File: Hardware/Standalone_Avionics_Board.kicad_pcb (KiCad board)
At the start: 4 copper layers, 112.4 x 57.1 mm, 138 parts, among them J1 GPS_Ant, J2 Charges A/B Terminal, J3 Charges C/D Terminal, J4 RF_Ant, J5 3-Pin Molex Power, J6 10118192-0001LF, J7 ARM 10 Pin, Q1 SI1040X-T1-GE3, Q2 SI7232DN-T1-GE3, Q3 SI7232DN-T1-GE3, U1 Si4463, U10 LM317T, U11 USBLC6-2SC6, U12 STM32L562VET, U13 W25Q32JVSS, U2 Si4463, U3 RSD-897.500-942.500-1612-TR, U4 ADL5521, U5 MS5607-02BA, U6 MAX-8Q, U7 KX134-1211, U8 MCP9808_MSOP, U9 BNO055, Y1 30MHz, Y2 30MHz, Y3 32.768kHz, Y4 32MHz

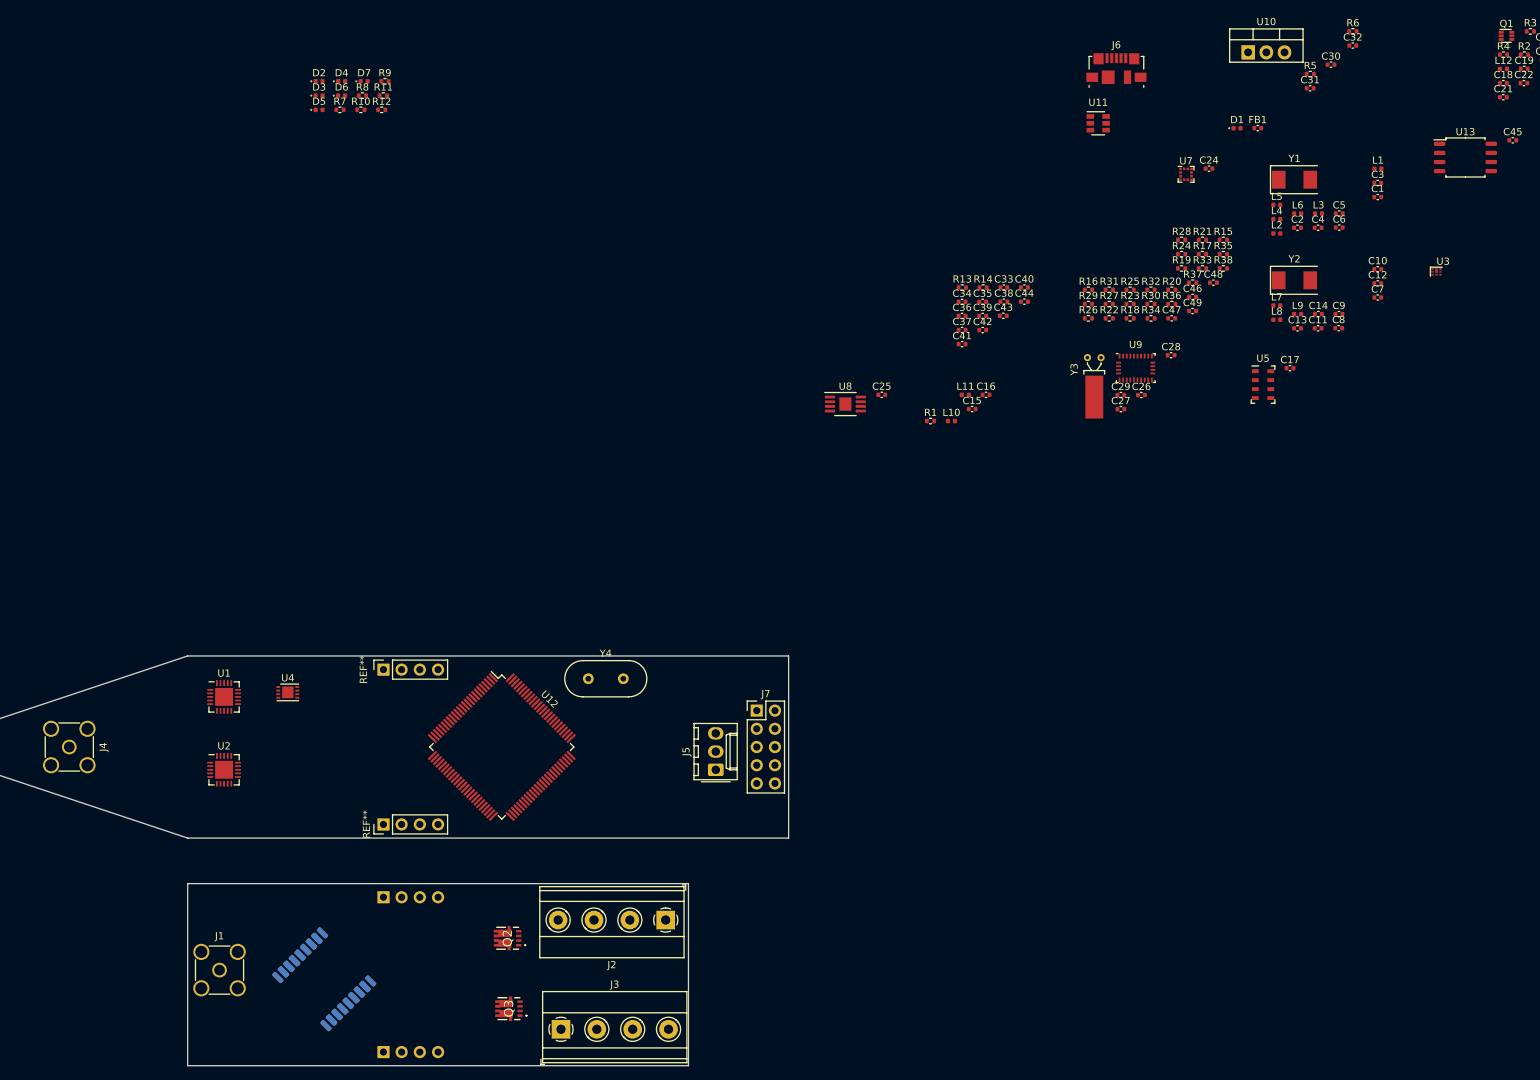
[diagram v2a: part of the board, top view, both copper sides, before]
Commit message: Added traces for I2C sensors
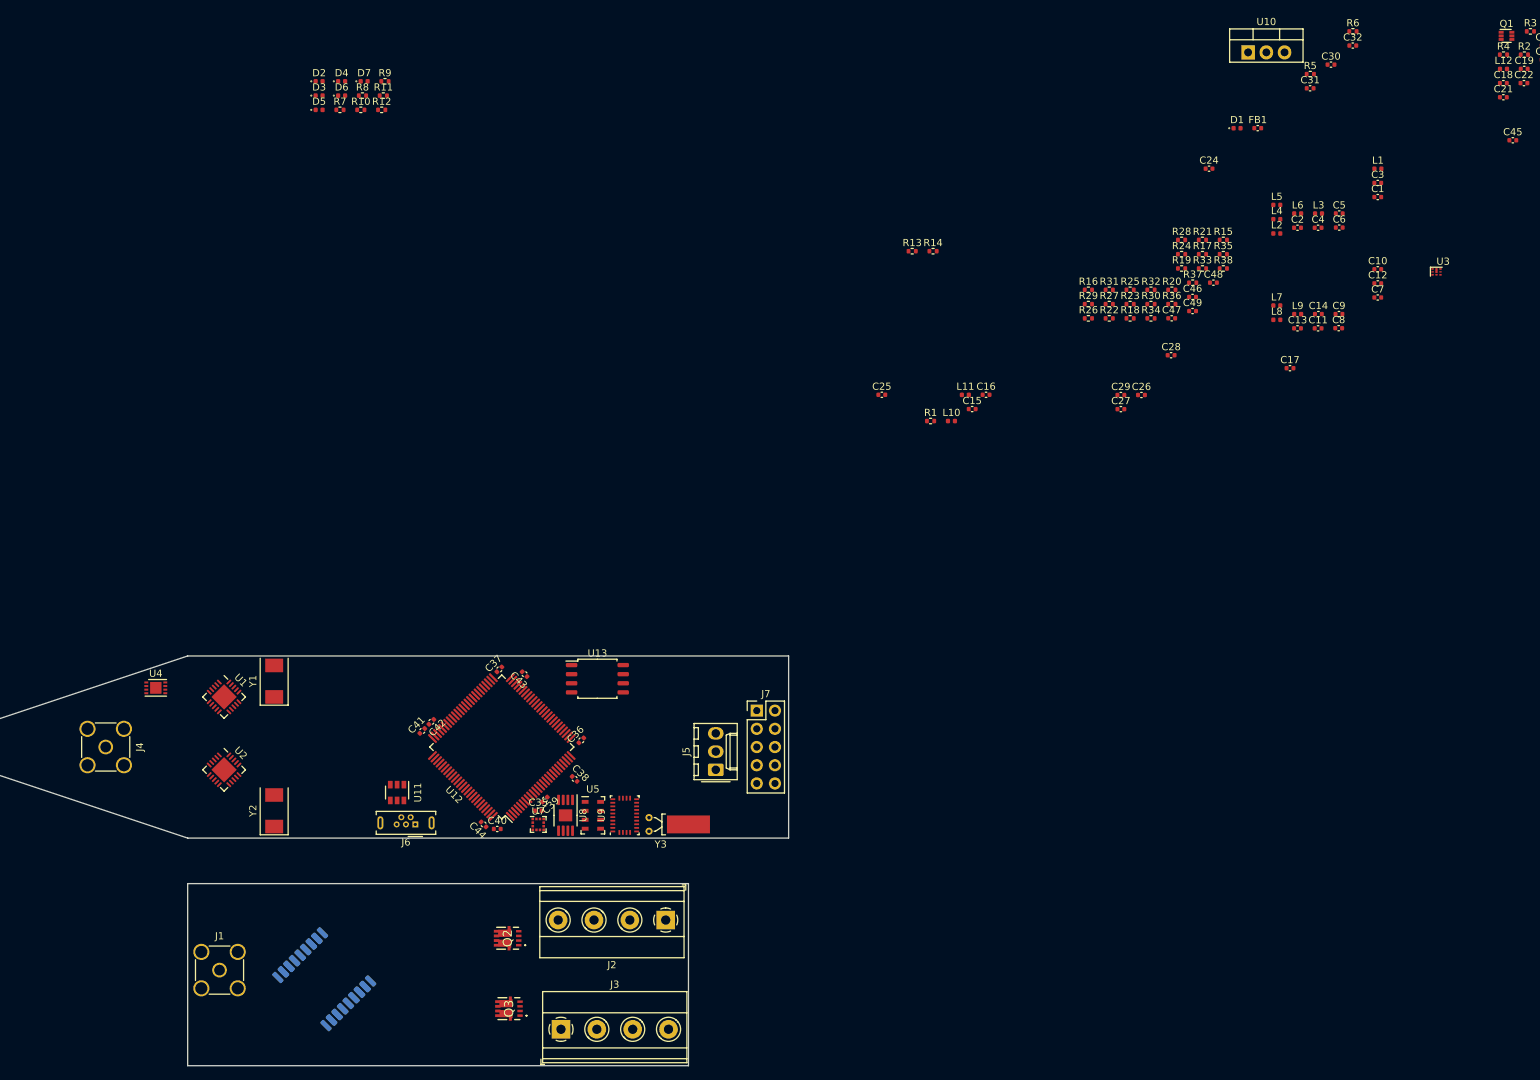
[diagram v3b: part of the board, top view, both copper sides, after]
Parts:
- removed C33, C34: 30pF, Capacitor_SMD:C_0402_1005Metric
- removed REF** (x2): PinHeader_1x04_P2.54mm_Vertical, Connector_PinHeader_2.54mm:PinHeader_1x04_P2.54mm_Vertical
- removed REF** (x2): PinSocket_1x04_P2.54mm_Vertical, Connector_PinSocket_2.54mm:PinSocket_1x04_P2.54mm_Vertical
- removed Y4: 32MHz, Crystal:Crystal_HC49-4H_Vertical
- J6: footprint Connector_USB:USB_Micro-B_Molex_47346-0001 -> Connector_USB:USB_Micro-B_Wuerth_614105150721_Vertical
- moved Y2 160.4 mm to (101.0, 129.5), turned to 90 degrees
- moved Y1 158.6 mm to (101.0, 111.5), turned to 90 degrees
- moved J6 143.8 mm to (120.7, 131.4), turned to 180 degrees
- moved U13 141.2 mm to (146.1, 111.1)
- moved U11 135.2 mm to (118.1, 127.0), turned to 270 degrees
- moved U7 128.0 mm to (137.8, 131.4)
- moved U5 111.1 mm to (145.4, 130.2)
- moved C40 105.4 mm to (132.1, 132.1)
- moved C44 104.9 mm to (130.2, 131.4), turned to 135 degrees
- moved U9 94.7 mm to (149.9, 130.2), turned to 90 degrees
- moved C42 94.3 mm to (122.9, 117.1), turned to 225 degrees
- moved C35 94.2 mm to (137.8, 129.5)
- moved C41 92.6 mm to (121.6, 118.4), turned to 45 degrees
- moved C39 91.0 mm to (138.7, 128.0), turned to 225 degrees
- moved Y3 90.0 mm to (153.2, 132.4), turned to 90 degrees
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
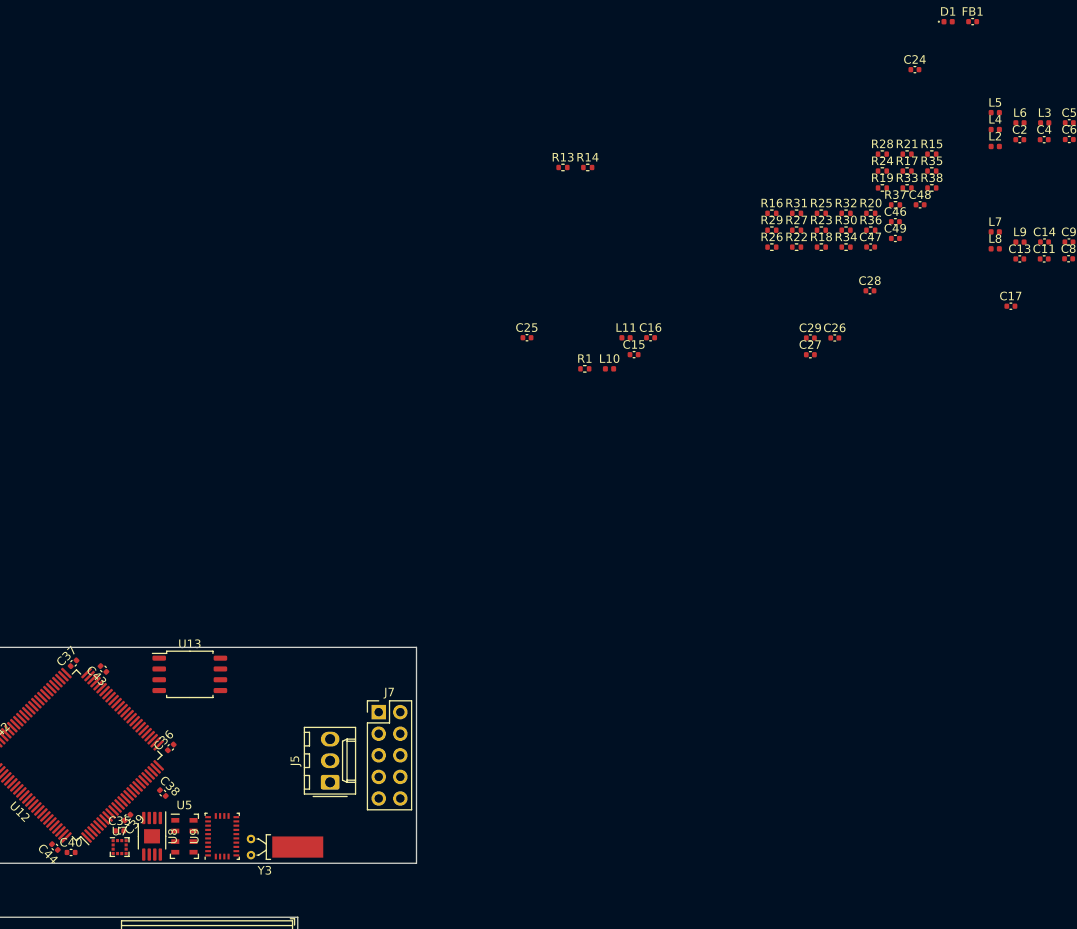
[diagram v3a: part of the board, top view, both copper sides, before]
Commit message: Forced addresses for I2C devices
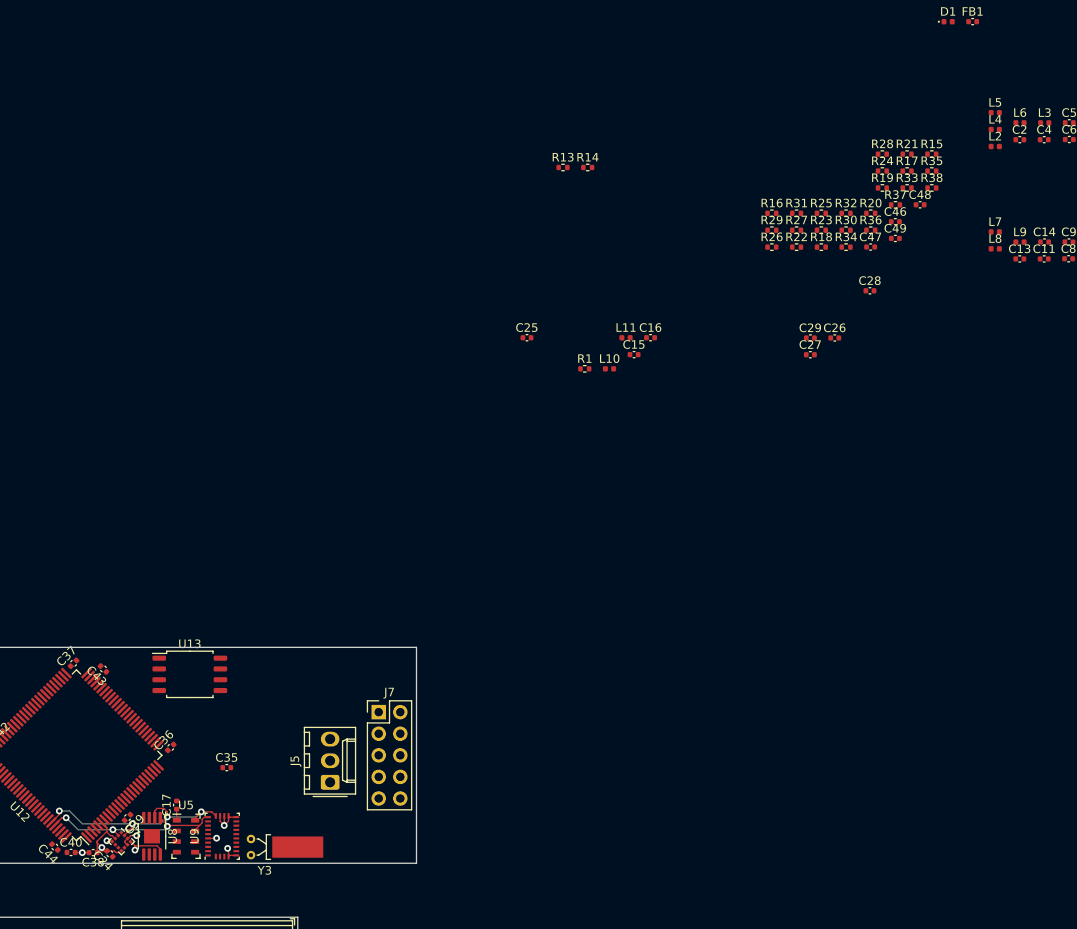
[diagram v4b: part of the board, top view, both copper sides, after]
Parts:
- moved C24 132.2 mm to (136.6, 132.2), turned to 135 degrees
- moved C17 114.4 mm to (144.5, 126.5), turned to 90 degrees
- moved C35 14.6 mm to (150.4, 122.1)
- moved C38 10.8 mm to (134.7, 132.1), turned to 180 degrees
- moved U7 0.68 mm to (138.0, 130.8), turned to 315 degrees
- moved U5 0.19 mm to (145.6, 130.2)
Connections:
- U5 pad 2: /MS5607/PS -> +3V3
- U5 pad 4: /MS5607/~CSB -> GND
- U5 pad 5: /MS5607/~CSB -> GND
- U5 pad 6: /MS5607/SDO -> GND
- U7 pad 9: Net-(U7-Pad9) -> GND
- U8 pad 5: /MCP9808/A2 -> GND
- U8 pad 6: /MCP9808/A1 -> GND
- U8 pad 7: /MCP9808/A0 -> GND
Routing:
- net /SENSORS_I2C_SCL: track 0.00 -> 28.3 mm, vias 0 -> 4
- net /SENSORS_I2C_SDA: track 0.00 -> 23.0 mm, vias 0 -> 3
- net +3V3: track 0.00 -> 16.1 mm, vias 0 -> 2
- net GND: track 0.00 -> 12.3 mm, vias 0 -> 6
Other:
- net class Minimum added: clearance 0.09, trace_width 0.09, via_dia 0.4, via_drill 0.2
- rule trace_min: 0.2 -> 0.09
- rule via_min_drill: 0.3 -> 0.2

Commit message: Board Layout Progress
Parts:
- moved J6 20.5 mm to (104.5, 118.8)
- moved U11 10.6 mm to (111.9, 118.4)
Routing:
- net GND: track 12.3 -> 40.3 mm, vias 6 -> 10
- net +3V3: track 16.1 -> 26.3 mm, vias 2 -> 6
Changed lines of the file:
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@@
     (thickness 1.6)
     (drawings 22)
-    (tracks 113)
+    (tracks 170)
     (zones 0)
     (modules 131)
@@
   )
   (module Connector_USB:USB_Micro-B_Wuerth_614105150721_Vertical (layer F.Cu)
-    (at 120.65 131.445 180)
+    (at 104.55 118.75 180)
     (descr "USB Micro-B receptacle, through-hole, vertical, http://katalog.we-online.de/em/datasheet/614105150721.pdf")
     (tags "usb micro receptacle vertical")
@@
   )
   (module Package_TO_SOT_SMD:SOT-23-6 (layer F.Cu)
-    (at 118.11 127 270)
+    (at 111.9 118.4 270)
     (descr "6-pin SOT-23 package")
     (tags SOT-23-6)
@@
   (segment (start 139.1 130.1) (end 139.8 130.1) (width 0.09) (layer F.Cu) (net 1))
   (segment (start 138.762392 130.437608) (end 139.1 130.1) (width 0.09) (layer F.Cu) (net 1))
+  (via (at 139.7 132.7) (size 0.8) (drill 0.4) (layers F.Cu B.Cu) (net 1))
+  (via (at 145.6 131.5) (size 0.8) (drill 0.4) (layers F.Cu B.Cu) (net 1))
+  (segment (start 144.9 130.8) (end 145.6 131.5) (width 0.09) (layer F.Cu) (net 1))
+  (segment (start 144.525 130.8) (end 144.9 130.8) (width 0.09) (layer F.Cu) (net 1))
+  (segment (start 145.05 132.05) (end 145.6 131.5) (width 0.09) (layer F.Cu) (net 1))
+  (segment (start 144.525 132.05) (end 145.05 132.05) (width 0.09) (layer F.Cu) (net 1))
+  (segment (start 146.15 132.05) (end 145.6 131.5) (width 0.09) (layer F.Cu) (net 1))
+  (segment (start 146.675 132.05) (end 146.15 132.05) (width 0.09) (layer F.Cu) (net 1))
+  (segment (start 146.3 130.8) (end 145.6 131.5) (width 0.09) (layer F.Cu) (net 1))
+  (segment (start 146.675 130.8) (end 146.3 130.8) (width 0.09) (layer F.Cu) (net 1))
+  (segment (start 140 133) (end 139.7 132.7) (width 0.09) (layer F.Cu) (net 1))
+  (segment (start 141.95 133) (end 140 133) (width 0.09) (layer F.Cu) (net 1))
+  (segment (start 140.63 129.27) (end 139.8 130.1) (width 0.09) (layer F.Cu) (net 1))
+  (segment (start 140.63 128.025) (end 140.63 129.27) (width 0.09) (layer F.Cu) (net 1))
+  (segment (start 139.875 130.175) (end 139.8 130.1) (width 0.09) (layer F.Cu) (net 1))
+  (segment (start 141.605 130.175) (end 139.875 130.175) (width 0.09) (layer F.Cu) (net 1))
+  (segment (start 138.257501 128.313822) (end 137.081384 127.137705) (width 0.09) (layer F.Cu) (net 1))
+  (segment (start 138.386178 128.313822) (end 138.257501 128.313822) (width 0.09) (layer F.Cu) (net 1))
+  (segment (start 138.386178 129.335484) (end 137.991161 129.730501) (width 0.09) (layer F.Cu) (net 1))
+  (segment (start 138.386178 128.313822) (end 138.386178 129.335484) (width 0.09) (layer F.Cu) (net 1))
+  (via (at 136.4 125.8) (size 0.8) (drill 0.4) (layers F.Cu B.Cu) (net 1))
+  (segment (start 136.4 126.456321) (end 136.4 125.8) (width 0.09) (layer F.Cu) (net 1))
+  (segment (start 137.081384 127.137705) (end 136.4 126.456321) (width 0.09) (layer F.Cu) (net 1))
+  (via (at 129.1 130.4) (size 0.8) (drill 0.4) (layers F.Cu B.Cu) (net 1))
+  (segment (start 129.13 130.4) (end 129.1 130.4) (width 0.09) (layer F.Cu) (net 1))
+  (segment (start 129.835589 131.105589) (end 129.13 130.4) (width 0.09) (layer F.Cu) (net 1))
+  (segment (start 130.036067 130.4) (end 129.1 130.4) (width 0.09) (layer F.Cu) (net 1))
+  (segment (start 130.823489 129.612578) (end 130.036067 130.4) (width 0.09) (layer F.Cu) (net 1))
+  (segment (start 140.63 127.46208) (end 140.63 128.025) (width 0.09) (layer F.Cu) (net 1))
+  (segment (start 142.07208 126.02) (end 140.63 127.46208) (width 0.09) (layer F.Cu) (net 1))
+  (segment (start 144.5 126.02) (end 142.07208 126.02) (width 0.09) (layer F.Cu) (net 1))
+  (segment (start 149.11 132.5625) (end 148.6725 133) (width 0.09) (layer F.Cu) (net 1))
+  (segment (start 147.625 133) (end 146.675 132.05) (width 0.09) (layer F.Cu) (net 1))
+  (segment (start 148.6725 133) (end 147.625 133) (width 0.09) (layer F.Cu) (net 1))
   (segment (start 144.5 128.275) (end 144.525 128.3) (width 0.09) (layer F.Cu) (net 2))
   (segment (start 144.5 126.98) (end 144.5 128.275) (width 0.09) (layer F.Cu) (net 2))
@@
   (segment (start 135.16 130.74) (end 135.6 130.3) (width 0.09) (layer F.Cu) (net 2))
   (segment (start 135.36 131.9) (end 135.16 132.1) (width 0.09) (layer F.Cu) (net 2))
-  (segment (start 136.3 131.9) (end 135.36 131.9) (width 0.09) (layer F.Cu) (net 2))
   (segment (start 135.16 132.1) (end 135.16 130.74) (width 0.09) (layer F.Cu) (net 2))
   (via (at 135.7 131.5) (size 0.8) (drill 0.4) (layers F.Cu B.Cu) (net 2))
-  (segment (start 135.16 130.96) (end 135.7 131.5) (width 0.09) (layer F.Cu) (net 2))
   (segment (start 135.16 130.74) (end 135.16 130.96) (width 0.09) (layer F.Cu) (net 2))
   (segment (start 139.069499 130.808839) (end 139.108839 130.808839) (width 0.09) (layer F.Cu) (net 2))
   (segment (start 139.6 131.3) (end 142.2 131.3) (width 0.09) (layer F.Cu) (net 2))
   (segment (start 139.108839 130.808839) (end 139.6 131.3) (width 0.09) (layer F.Cu) (net 2))
-  (via (at 139.6 131.8) (size 0.8) (drill 0.4) (layers F.Cu B.Cu) (net 2))
-  (segment (start 139.6 131.3) (end 139.6 131.8) (width 0.09) (layer F.Cu) (net 2))
+  (via (at 139.6 131.5) (size 0.8) (drill 0.4) (layers F.Cu B.Cu) (net 2))
+  (segment (start 139.6 131.3) (end 139.6 131.5) (width 0.09) (layer F.Cu) (net 2))
+  (via (at 143.4 130.1) (size 0.8) (drill 0.4) (layers F.Cu B.Cu) (net 2))
+  (segment (start 143.95 129.55) (end 143.4 130.1) (width 0.09) (layer F.Cu) (net 2))
+  (segment (start 144.525 129.55) (end 143.95 129.55) (width 0.09) (layer F.Cu) (net 2))
+  (segment (start 138.335 127.635) (end 139.065 127.635) (width 0.09) (layer F.Cu) (net 2))
+  (segment (start 137.484151 126.784151) (end 138.335 127.635) (width 0.09) (layer F.Cu) (net 2))
+  (segment (start 137.434938 126.784151) (end 137.484151 126.784151) (width 0.09) (layer F.Cu) (net 2))
+  (segment (start 136.1 131.9) (end 135.7 131.5) (width 0.09) (layer F.Cu) (net 2))
+  (segment (start 136.3 131.9) (end 136.1 131.9) (width 0.09) (layer F.Cu) (net 2))
+  (segment (start 135.7 131.56) (end 135.16 132.1) (width 0.09) (layer F.Cu) (net 2))
+  (segment (start 135.7 131.5) (end 135.7 131.56) (width 0.09) (layer F.Cu) (net 2))
+  (via (at 130.9 132.6) (size 0.8) (drill 0.4) (layers F.Cu B.Cu) (net 2))
+  (segment (start 131.42 132.08) (end 130.9 132.6) (width 0.09) (layer F.Cu) (net 2))
+  (segment (start 131.6 132.08) (end 131.42 132.08) (width 0.09) (layer F.Cu) (net 2))
+  (segment (start 130.514411 132.214411) (end 130.9 132.6) (width 0.09) (layer F.Cu) (net 2))
+  (segment (start 130.514411 131.784411) (end 130.514411 132.214411) (width 0.09) (layer F.Cu) (net 2))
+  (segment (start 131.530596 130.768226) (end 130.514411 131.784411) (width 0.09) (layer F.Cu) (net 2))
+  (segment (start 131.530596 130.319685) (end 131.530596 130.768226) (width 0.09) (layer F.Cu) (net 2))
+  (via (at 145.65 127) (size 0.8) (drill 0.4) (layers F.Cu B.Cu) (net 2))
+  (segment (start 145.63 126.98) (end 145.65 127) (width 0.09) (layer F.Cu) (net 2))
+  (segment (start 144.5 126.98) (end 145.63 126.98) (width 0.09) (layer F.Cu) (net 2))
+  (via (at 149.3 131.55) (size 0.8) (drill 0.4) (layers F.Cu B.Cu) (net 2))
+  (segment (start 149.61 131.86) (end 149.3 131.55) (width 0.09) (layer F.Cu) (net 2))
+  (segment (start 149.61 132.5625) (end 149.61 131.86) (width 0.09) (layer F.Cu) (net 2))
+  (segment (start 148.925 131.925) (end 149.3 131.55) (width 0.09) (layer F.Cu) (net 2))
+  (segment (start 148.1975 131.925) (end 148.925 131.925) (width 0.09) (layer F.Cu) (net 2))
   (segment (start 129.762829 128.551918) (end 129.762829 128.537171) (width 0.09) (layer F.Cu) (net 56))
   (via (at 130.7 127.2) (size 0.8) (drill 0.4) (layers F.Cu B.Cu) (net 56))
